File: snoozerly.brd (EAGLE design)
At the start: 70 x 43 mm, 57 parts, among them Q2 MOSFET-NCHANNELFDD8780, Q3 MOSFET-NCHANNELBSS123LT1G, Q4 MOSFET-NCHANNELBSS123LT1G, U1 ATMEGA328P, Y1 32KHz, Y2 8MHz

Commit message: fixed touch sensor vcc and gnd. increased docu fonts.
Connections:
- net 5V: now also AT42QT1070.1; no longer AT42QT1070.14
- net GND: now also AT42QT1070.14; no longer AT42QT1070.1
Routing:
- net 5V: track 193.2 -> 190.3 mm, vias 8 -> 6
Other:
- board text added: "VDD"

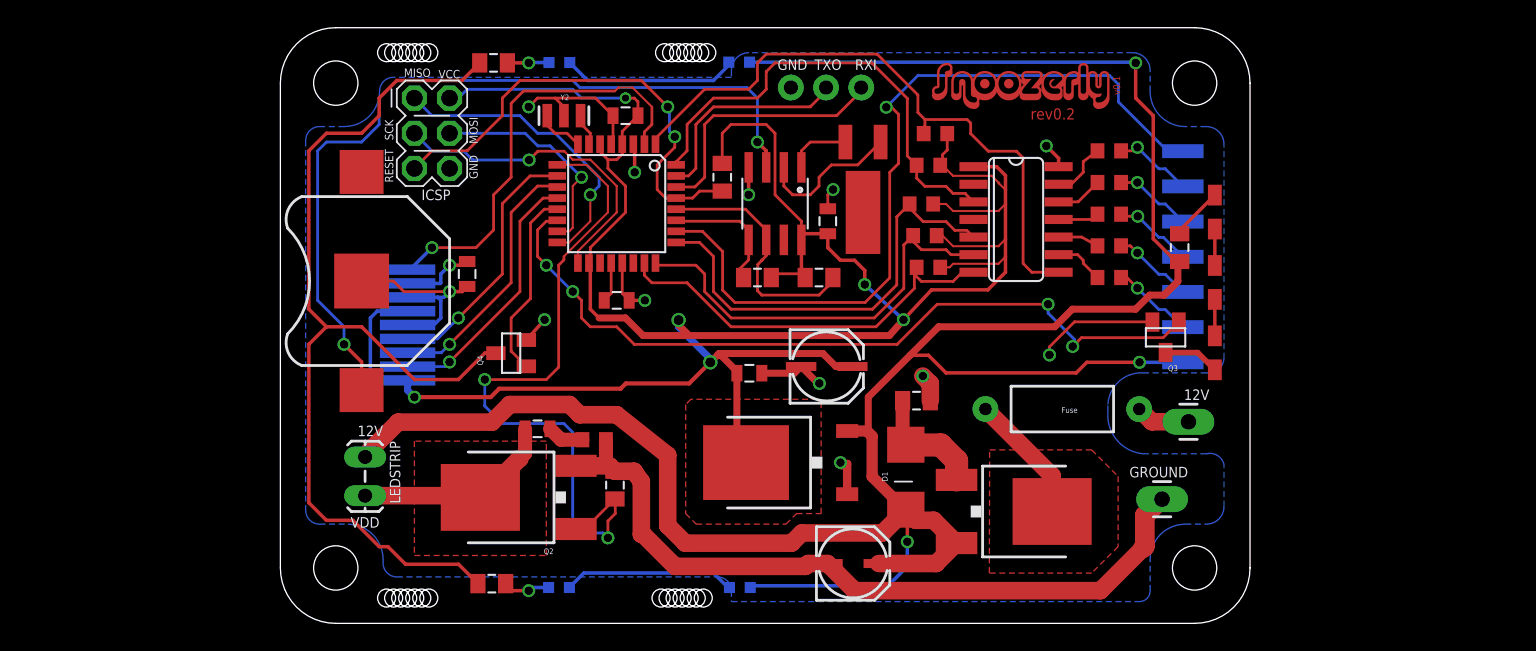
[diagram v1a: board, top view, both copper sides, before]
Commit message: updates before touch sensor changes.
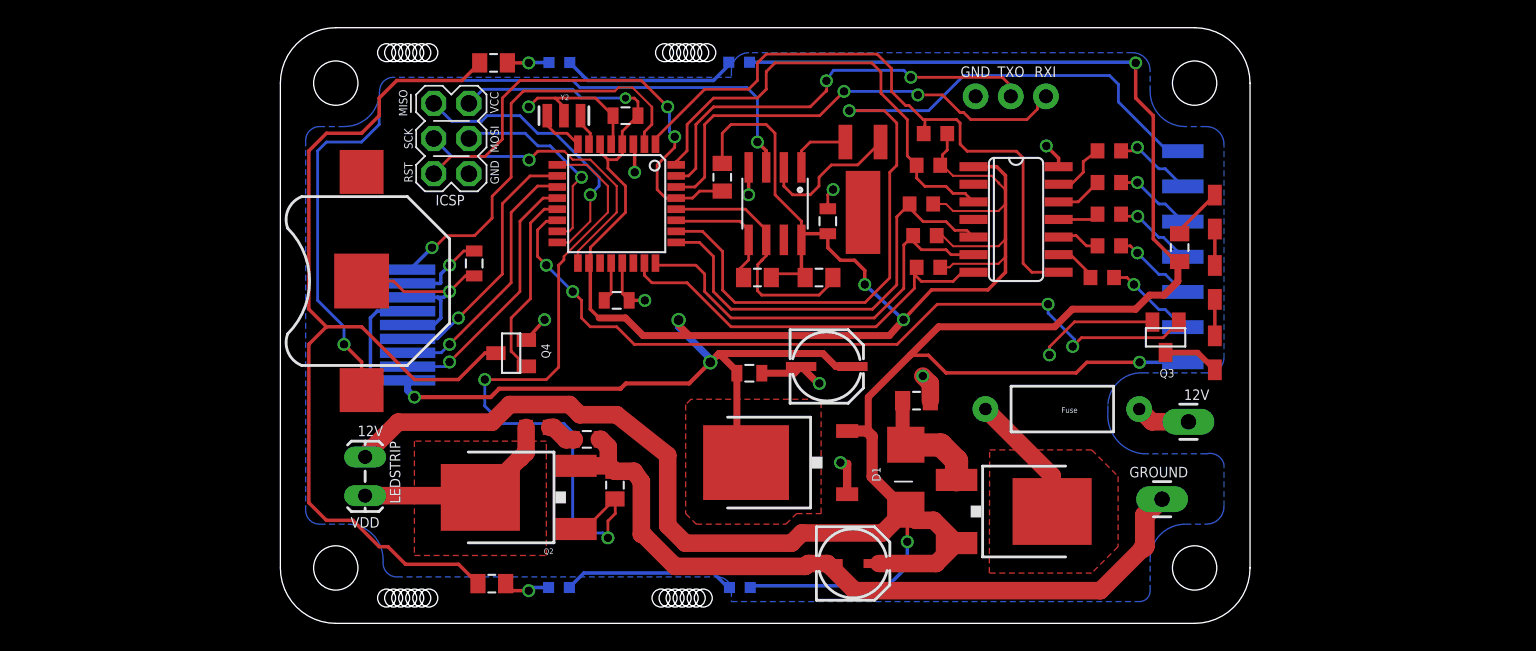
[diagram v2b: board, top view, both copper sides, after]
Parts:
- removed U$19: (no value), jt_parts:SNOOZERLY_TOP
- C1, C2, C3, C6: value 100nF -> 0.1uF
- moved SERIAL 13.4 mm to (50.6, 38.5)
- moved U$25 4.16 mm to (19.1, 14.6)
- moved C4 3.64 mm to (22.6, 13.7)
- moved ICSP 1.45 mm to (11.5, 38.0)
- moved C6 0.92 mm to (14.5, 26.4)
- moved U$11 0.51 mm to (59.8, 25.4)
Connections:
- net GND: now also C4.1; no longer U$25.1
- net N$14: now also U$25.2; no longer C4.2
- net N$18: now also C4.2, U$25.1; no longer C4.1, U$25.2
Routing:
- net TXO: track 15.5 -> 31.1 mm, vias 0 -> 2
- net RXI: track 18.7 -> 33.5 mm, vias 0 -> 2
- net STATUS: track 58.5 -> 63.2 mm
- net SCK: track 23.4 -> 21.9 mm
- net GND: track 112.5 -> 113.7 mm
- net 5V: track 190.3 -> 189.0 mm
- net MOSI: track 16.0 -> 14.7 mm
- net MISO: track 22.2 -> 20.9 mm
- net N$20: track 5.33 -> 6.15 mm
- net OUT1: track 46.0 -> 46.7 mm
- net N$14: track 16.6 -> 17.2 mm
- net /RES: track 31.2 -> 30.6 mm
- net N$21: track 5.95 -> 6.45 mm
- net N$18: track 2.67 -> 2.16 mm
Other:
- board text added: "RST"
- board text removed: "RESET"
- board text removed: "rev0.2"
- board text removed: "v0.1"

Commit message: increase drill size change remaining.
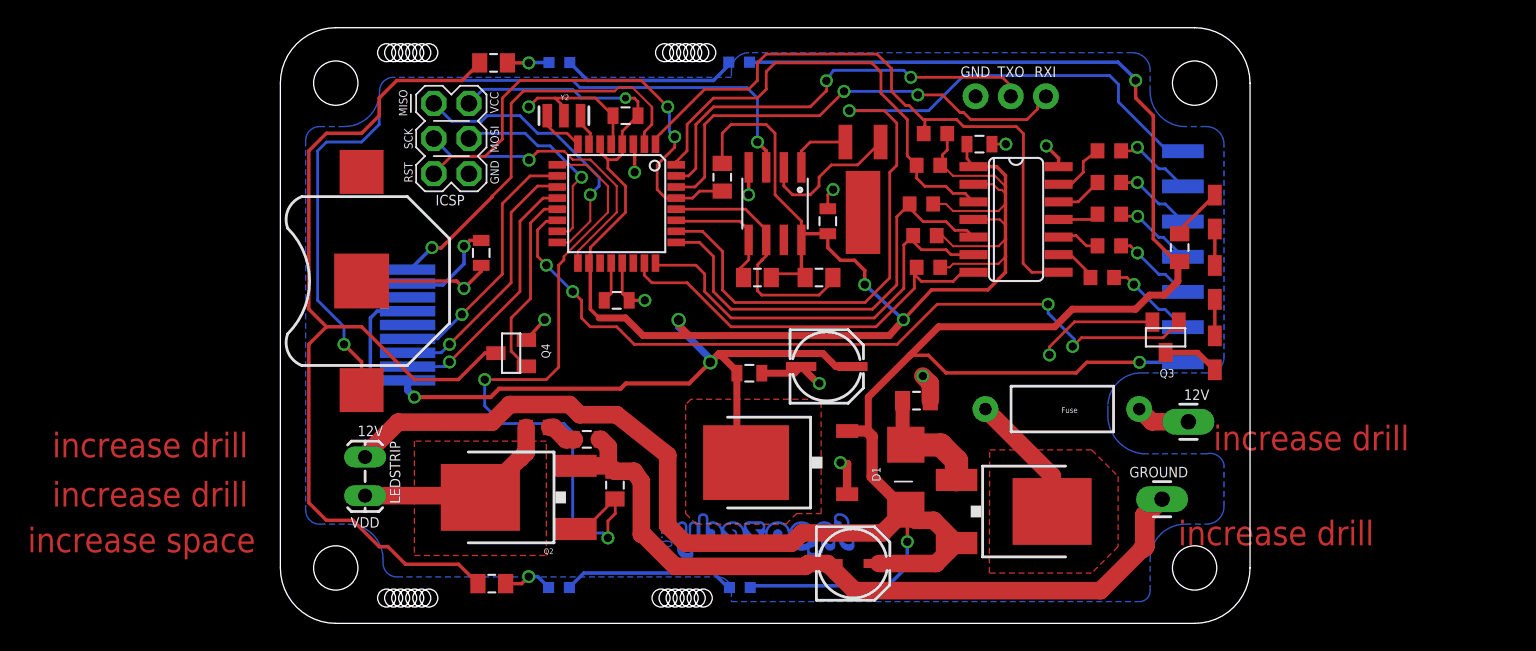
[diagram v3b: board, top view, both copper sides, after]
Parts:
- added C9: 0.1uF, SparkFun-Capacitors:0805
- added U$19: (no value), jt_parts:SNOOZERLY_TOP
- C1: value 0.1uF -> 100nF
- moved C6 0.92 mm to (15.0, 27.2)
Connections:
- net 5V: now also AT42QT1070.2, AT42QT1070.4, C9.1
- net GND: now also C9.2
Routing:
- net 5V: track 189.0 -> 195.8 mm
- net GND: track 113.7 -> 108.1 mm, vias 12 -> 13
- net N$20: track 6.15 -> 7.43 mm
- net 12V: track 179.3 -> 178.6 mm
- net /RES: track 30.6 -> 29.9 mm
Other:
- board text added: "increase drill"
- board text added: "increase space"

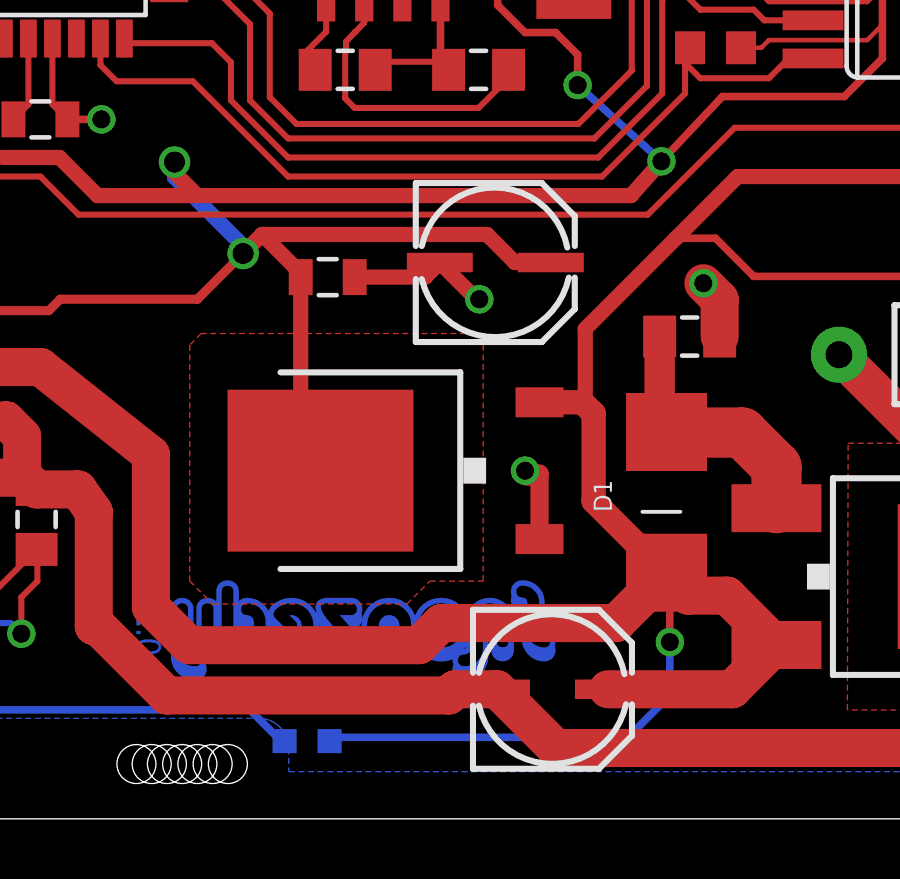
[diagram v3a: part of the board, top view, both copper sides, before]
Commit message: increased 10uf cap pads
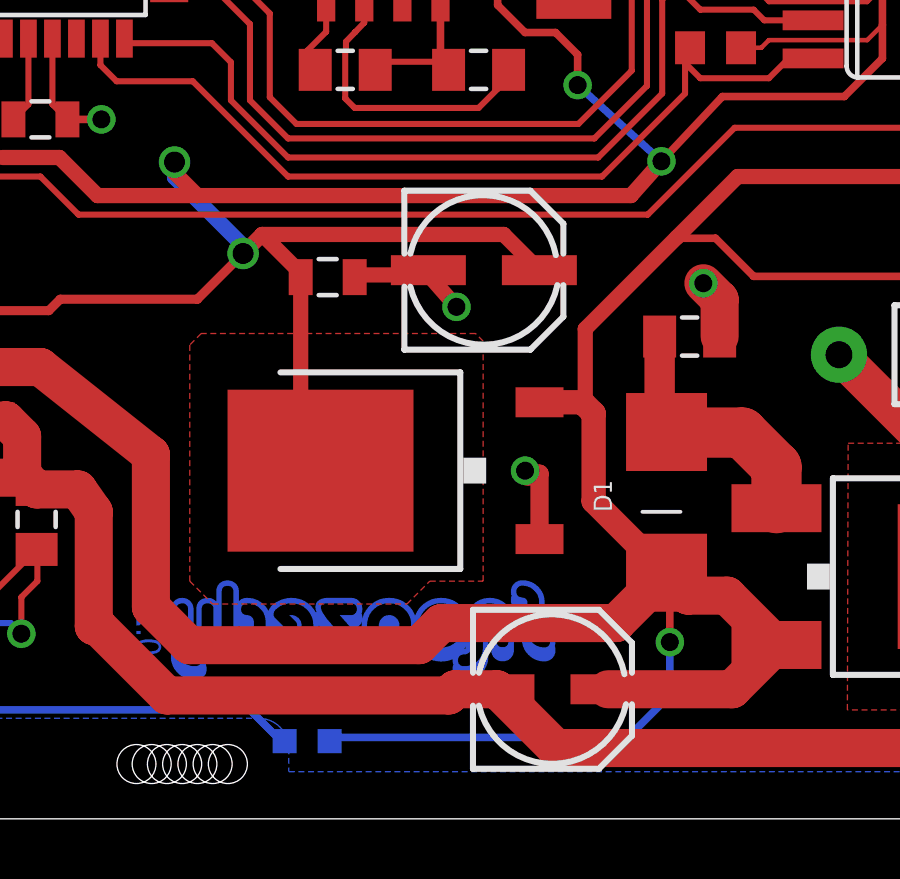
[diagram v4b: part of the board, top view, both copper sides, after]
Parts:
- C5, C7: device SparkFun-Capacitors:PANASONIC_C -> jt_parts:CAP-PANASONIC-C
- moved C7 0.46 mm to (39.5, 18.9)
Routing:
- net GND: track 108.1 -> 107.3 mm
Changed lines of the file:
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@@
 <setting verticaltext="up"/>
 </settings>
-<grid distance="10" unitdist="mil" unit="mil" style="dots" multiple="1" display="yes" altdistance="5" altunitdist="mil" altunit="mil"/>
+<grid distance="25" unitdist="mil" unit="mil" style="dots" multiple="1" display="yes" altdistance="5" altunitdist="mil" altunit="mil"/>
 <layers>
 <layer number="1" name="Top" color="4" fill="1" visible="yes" active="yes"/>
@@
 <attribute name="LED3" x="66.6496" y="20.7264" size="0.4064" layer="27" ratio="10" rot="R270" display="name"/>
 </element>
-<element name="C5" library="SparkFun-Capacitors" package="PANASONIC_C" value="10uF" x="41.7576" y="4.9784" smashed="yes">
+<element name="C5" library="jt_parts" package="CAP-PANASONIC-C" value="10uF" x="41.7576" y="4.9784" smashed="yes">
 <attribute name="VALUE" x="41.4036" y="5.2944" size="0.6096" layer="27"/>
 </element>
-<element name="C7" library="SparkFun-Capacitors" package="PANASONIC_C" value="10uF" x="39.8526" y="19.2024" smashed="yes">
-<attribute name="VALUE" x="39.4986" y="19.5184" size="0.6096" layer="27"/>
+<element name="C7" library="jt_parts" package="CAP-PANASONIC-C" value="10uF" x="39.4716" y="18.9484" smashed="yes">
+<attribute name="VALUE" x="39.1176" y="19.2644" size="0.6096" layer="27"/>
 </element>
 <element name="C2" library="SparkFun-Capacitors" package="0805" value="0.1uF" x="25.3746" y="37.1094" smashed="yes" rot="R180">
@@
 <via x="40.894" y="12.065" extent="1-16" drill="0.6"/>
 <wire x1="40.995" y1="11.964" x2="40.894" y2="12.065" width="0.8128" layer="1"/>
-<wire x1="35.2154" y1="18.5166" x2="37.5668" y2="18.5166" width="0.508" layer="1"/>
-<wire x1="37.5668" y1="18.5166" x2="38.0526" y2="19.0024" width="0.508" layer="1"/>
-<via x="39.37" y="17.78" extent="1-16" drill="0.6"/>
-<wire x1="39.37" y1="17.78" x2="39.275" y2="17.78" width="0.508" layer="1"/>
-<wire x1="39.275" y1="17.78" x2="38.0526" y2="19.0024" width="0.508" layer="1"/>
+<via x="38.608" y="17.526" extent="1-16" drill="0.6"/>
 <wire x1="40.995" y1="11.964" x2="41.376" y2="11.964" width="0.6096" layer="1"/>
 <wire x1="41.376" y1="11.964" x2="41.376" y2="9.785" width="0.6096" layer="1"/>
@@
 <wire x1="14.9606" y1="26.3034" x2="14.9606" y2="25.8826" width="0.254" layer="1"/>
 <wire x1="14.9606" y1="25.8826" x2="13.716" y2="24.638" width="0.254" layer="1"/>
+<wire x1="38.608" y1="17.526" x2="37.6716" y2="18.5894" width="0.508" layer="1"/>
+<wire x1="37.6716" y1="18.5894" x2="37.6716" y2="18.7484" width="0.508" layer="1"/>
+<wire x1="37.6716" y1="18.5894" x2="35.2882" y2="18.5894" width="0.508" layer="1"/>
+<wire x1="35.2882" y1="18.5894" x2="35.2154" y2="18.5166" width="0.508" layer="1"/>
 <wire x1="64.1096" y1="9.4234" x2="64.1096" y2="9.4996" width="0" layer="19" extent="1-1"/>
 </signal>
@@
 <wire x1="21.5646" y1="39.0144" x2="22.1996" y2="38.3794" width="0.2032" layer="16"/>
 <wire x1="22.1996" y1="38.3794" x2="25.3746" y2="38.3794" width="0.2032" layer="16"/>
-<wire x1="39.624" y1="19.939" x2="32.131" y2="19.939" width="0.508" layer="1"/>
+<wire x1="40.181" y1="19.939" x2="32.131" y2="19.939" width="0.508" layer="1"/>
 <via x="31.496" y="19.304" extent="1-16" drill="0.7"/>
 <wire x1="31.496" y1="19.304" x2="31.496" y2="19.558" width="0.508" layer="16"/>
@@
 <wire x1="47.4726" y1="24.5364" x2="45.4406" y2="22.3774" width="0.254" layer="1"/>
 <contactref element="U$23" pad="1"/>
-<wire x1="41.7526" y1="19.0024" x2="41.7036" y2="19.0024" width="0.508" layer="1"/>
 <wire x1="48.602" y1="35.814" x2="48.602" y2="34.632" width="0.2032" layer="1"/>
 <wire x1="48.602" y1="34.632" x2="48.26" y2="34.29" width="0.2032" layer="1"/>
@@
 <wire x1="16.256" y1="17.399" x2="25.019" y2="17.399" width="0.3048" layer="1"/>
 <wire x1="25.019" y1="17.399" x2="25.4" y2="17.78" width="0.3048" layer="1"/>
-<wire x1="41.7036" y1="19.0024" x2="41.3226" y2="19.0024" width="0.4064" layer="1"/>
 <wire x1="32.131" y1="19.939" x2="31.496" y2="19.304" width="0.508" layer="1"/>
 <wire x1="25.4" y1="17.78" x2="29.972" y2="17.78" width="0.3048" layer="1"/>
 <wire x1="29.972" y1="17.78" x2="31.496" y2="19.304" width="0.3048" layer="1"/>
 <contactref element="NCP1117" pad="2"/>
-<wire x1="41.3226" y1="19.0024" x2="40.5606" y2="19.0024" width="0.508" layer="1"/>
-<wire x1="40.5606" y1="19.0024" x2="39.624" y2="19.939" width="0.508" layer="1"/>
 <wire x1="33.4154" y1="18.5166" x2="33.4154" y2="18.6546" width="0.508" layer="1"/>
 <wire x1="33.4154" y1="18.6546" x2="32.131" y2="19.939" width="0.508" layer="1"/>
@@
 <wire x1="50.027" y1="35.052" x2="50.027" y2="34.0216" width="0.2032" layer="1"/>
 <wire x1="50.027" y1="34.0216" x2="50.4952" y2="33.4264" width="0.2032" layer="1"/>
+<wire x1="40.181" y1="19.939" x2="41.3716" y2="18.7484" width="0.508" layer="1"/>
 </signal>
 <signal name="N$64">
